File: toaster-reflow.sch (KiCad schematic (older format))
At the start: 20 parts, among them J1 1935161, J2 1935161, J3 Raspberry_Pi_2_3, J4 Conn_01x04, J6 Conn_01x03, K1 1-1415899-3, Q1 Q_NMOS_GSD, Q2 Q_NMOS_GSD, U1 3.3V Ref

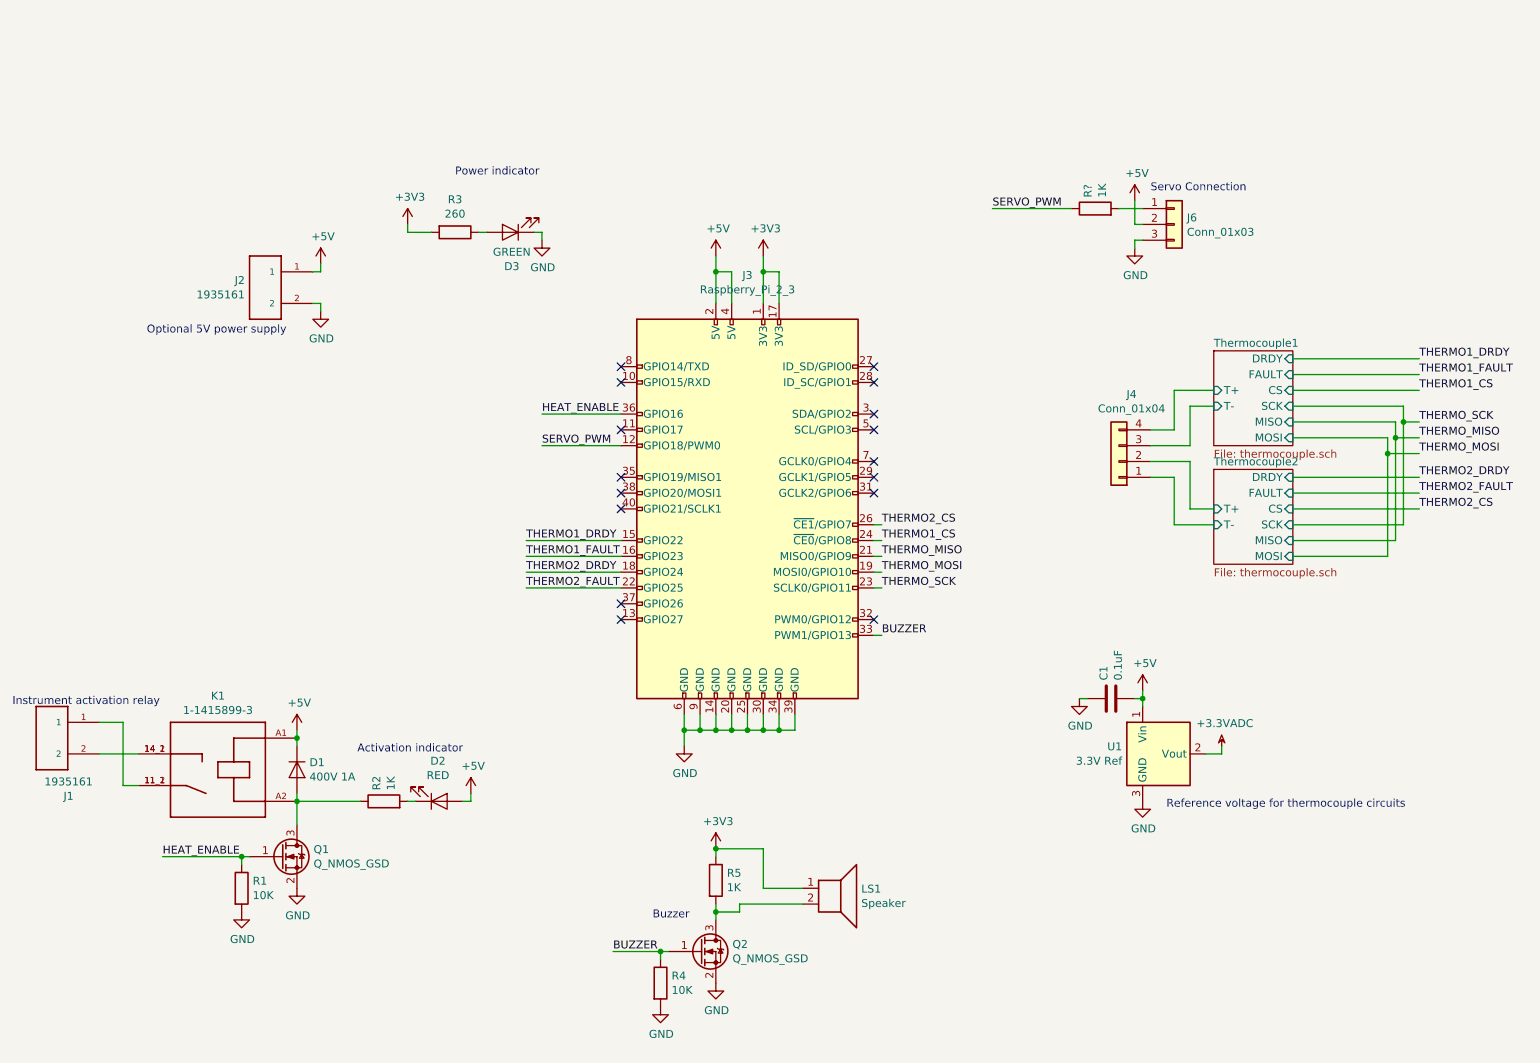
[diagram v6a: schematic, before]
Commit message: new design/ layout
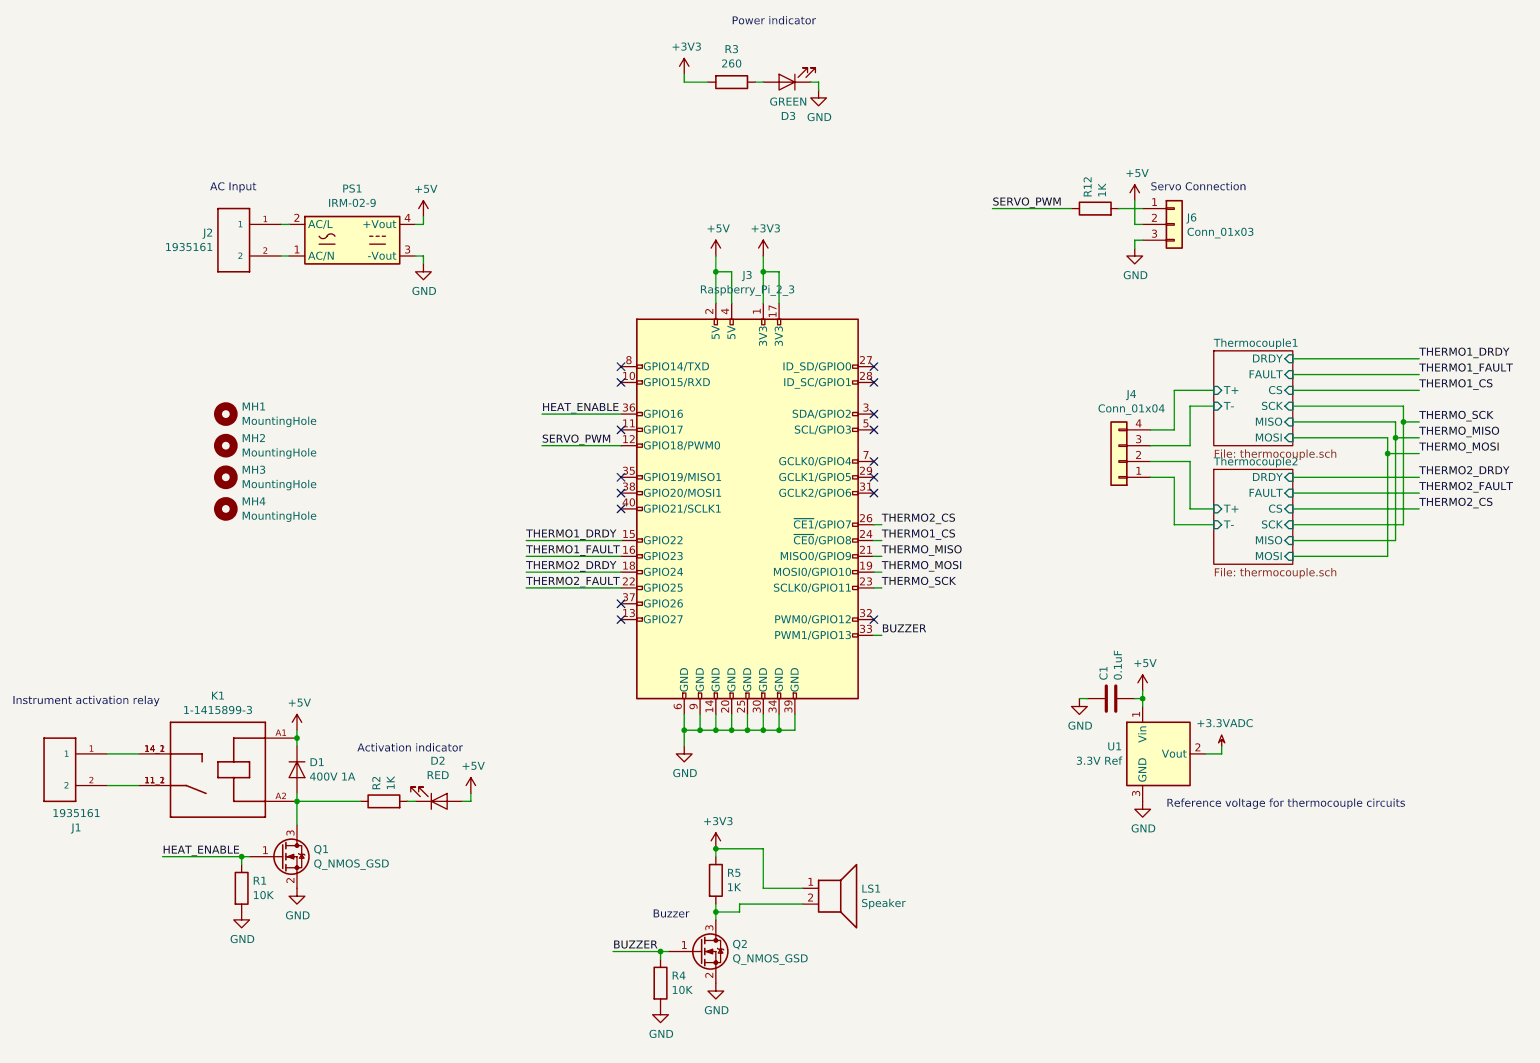
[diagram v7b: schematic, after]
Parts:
- added MH1, MH2, MH3, MH4: MountingHole, MountingHole:MountingHole_2.7mm_M2.5, symbol Mechanical:MountingHole
- added PS1: IRM-02-9, custom:IRM-15-5, symbol Converter_ACDC:IRM-02-9
- gave numbers to parts that had none: 1
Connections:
- net +5V: now also PS1.4 (+Vout); no longer J2.1
- net GND: now also PS1.3 (-Vout); no longer J2.2
- net at K1.11_1 (11), K1.11_2 (11): now also J1.2; no longer J1.1
- net at K1.14_1 (14), K1.14_2 (14): now also J1.1; no longer J1.2
- new net: J2.1, PS1.2 (AC/L)
- new net: J2.2, PS1.1 (AC/N)
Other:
- note added: "AC Input"
- note removed: "Optional 5V power supply\n"
- moved on the sheet: D3, J1, J2, R3
